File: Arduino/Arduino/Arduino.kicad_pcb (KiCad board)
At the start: 2 copper layers, 98 parts, among them J1 Conn_01x08_Socket, J10 USB_B_Mini, J2 Conn_01x08_Socket, J3 Conn_01x06_Socket, J4 Conn_01x10_Socket, J5 Conn_01x02_Socket, J6 Conn_02x03_Odd_Even, J7 Conn_02x03_Odd_Even, J8 Conn_01x02_Socket, J9 Conn_01x02_Socket, P1 USB_C_Plug_USB2.0, Q1 MMBT3904, Q2 MMBT3904, Q3 MMBT3904, Q4 MMBT3904, Q5 MMBT3904, Q6 MMBT3904, SW1 SW_Push, SW2 SW_Push, SW3 SW_Push, SW4 SW_Push, SW5 SW_Push, SW6 SW_Push, U1 LM1117DT-3.3, U2 TPS61087DSCR, U3 FT232RL, U4 ATxmega32A4U-A, U5 HC-05, U6 L293D

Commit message: Primera versión del Arduino sin completar el Ruteo
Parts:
- removed P1: USB_C_Plug_USB2.0, Connector_USB:USB_C_Receptacle_GCT_USB4125-xx-x_6P_TopMnt_Horizontal
- added H1: MountingHole_Pad, MountingHole:MountingHole_3.2mm_M3_DIN965_Pad, F.Cu at (205.0, 32.5)
- added H2: MountingHole_Pad, MountingHole:MountingHole_3.2mm_M3_DIN965_Pad, F.Cu at (256.3, 47.7)
- added H3: MountingHole_Pad, MountingHole:MountingHole_3.2mm_M3_DIN965_Pad, F.Cu at (256.4, 75.7)
- added H4: MountingHole_Pad, MountingHole:MountingHole_3.2mm_M3_DIN965_Pad, F.Cu at (204.3, 80.8)
- C14, C6, C7, D1, D2, R1, R10, R11, R14, R15, R16, R17, R18, R19, R2, R20, R21, R22, R23, R24, R25, R26, R27, R28, R29, R3, R30, R31, R32, R33, R34, R35, R36, R4, R5, R6, R7, R8, R9, U1, U3: moved to B.Cu
- D5: footprint Diode_SMD:D_SMC -> Diode_SMD:D_SMA; moved to B.Cu
- SW1, SW2, SW3, SW4, SW5, SW6: footprint Button_Switch_THT:SW_Tactile_Straight_KSA0Axx1LFTR -> Button_Switch_SMD:SW_SPST_EVQP2_MiddlePushTravel_H2.5mm
- moved SW6 161.7 mm to (250.0, 68.0)
- moved SW5 161.3 mm to (250.0, 62.7)
- moved SW4 160.9 mm to (250.0, 57.4)
- moved SW3 160.6 mm to (250.0, 52.1)
- moved RV1 157.7 mm to (239.8, 51.3), turned to -90 degrees
- moved SW1 141.2 mm to (230.6, 53.8), turned to 90 degrees
- moved J10 131.4 mm to (196.2, 35.9), turned to -90 degrees
- moved J6 131.3 mm to (246.0, 37.0), turned to 90 degrees
- moved C15 126.9 mm to (256.4, 52.1), turned to -90 degrees
- moved J8 126.8 mm to (251.8, 75.7), turned to 180 degrees
- moved C16 126.5 mm to (256.4, 57.4), turned to -90 degrees
- moved C17 126.2 mm to (256.4, 62.7), turned to -90 degrees
- moved C18 126.0 mm to (256.4, 68.0), turned to -90 degrees
- moved R26 125.8 mm to (256.4, 52.1), turned to -90 degrees
- moved D13 125.7 mm to (208.1, 58.4)
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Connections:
- C3 pad 1: Net-(D5-K) -> +12V
- D5 pad 1: Net-(D5-K) -> +12V
- R4 pad 1: Net-(D5-K) -> +12V
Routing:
- net +5V: track 0.00 -> 120.1 mm, vias 0 -> 3
- net +3.3V: track 0.00 -> 107.1 mm, vias 0 -> 1
- net +12V: track 0.00 -> 53.9 mm, vias 0 -> 1
- net /RESET: track 0.00 -> 48.3 mm
- net /PD0: track 0.00 -> 28.3 mm
- net /3A: track 0.00 -> 19.2 mm, vias 0 -> 2
- net VBUS: track 0.00 -> 17.5 mm, vias 0 -> 2
- net Net-(J9-Pin_1): track 0.00 -> 13.5 mm
- net /2A: track 0.00 -> 12.7 mm, vias 0 -> 1
- net /1A: track 0.00 -> 10.4 mm, vias 0 -> 1
- net Net-(D5-A): track 0.00 -> 10.1 mm, vias 0 -> 1
- net Net-(U3-3V3OUT): track 0.00 -> 9.95 mm
- net Net-(U3-~{RESET}): track 0.00 -> 9.22 mm
- net /PD3: track 0.00 -> 9.03 mm
- net /PD2: track 0.00 -> 9.03 mm
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- added copper zone on B.Cu, net GND
- added copper zone on F.Cu, net GND
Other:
- board outline added: 68.8 x 53.6 mm

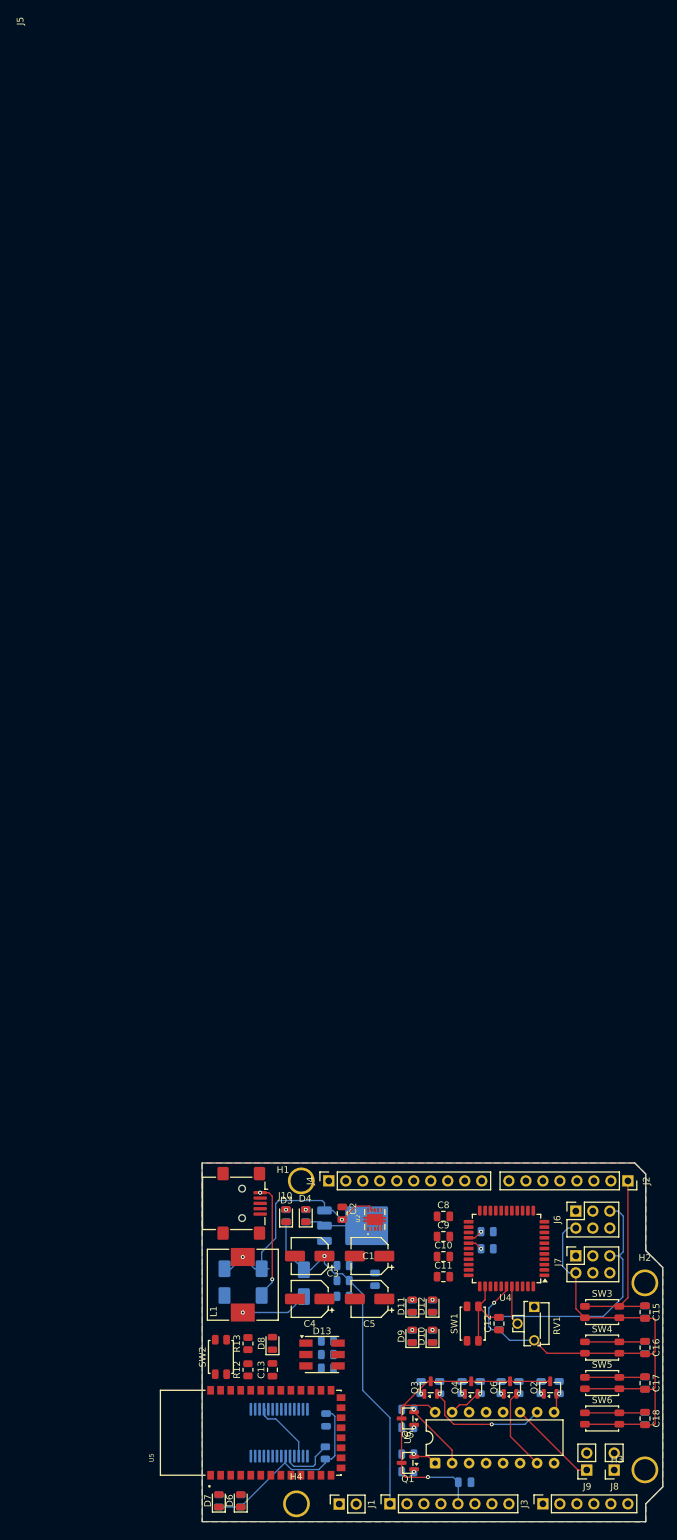
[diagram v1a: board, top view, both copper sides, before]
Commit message: Segunda Versión casi finalizada, falta enrutar detalles y gnd
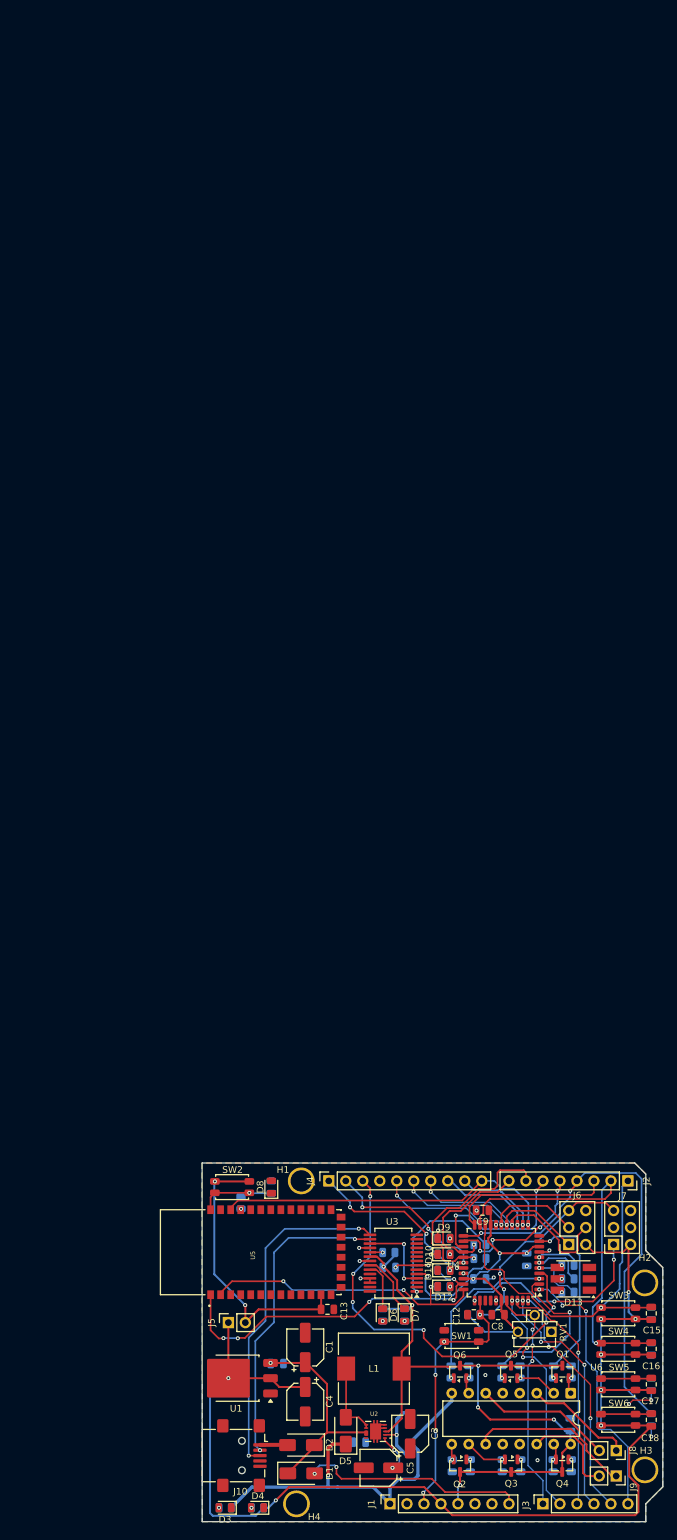
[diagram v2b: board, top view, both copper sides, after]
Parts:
- C10, C11, C2, R12, R13: moved to B.Cu
- D1, D2, D5, U1, U3: moved to F.Cu
- moved D3 44.6 mm to (193.6, 81.3), turned to 180 degrees
- moved R2 44.6 mm to (193.6, 81.3), turned to 180 degrees
- moved D4 44.3 mm to (198.4, 81.3), turned to 180 degrees
- moved R1 44.2 mm to (198.5, 81.3), turned to 180 degrees
- moved R8 39.3 mm to (220.4, 52.5), turned to -90 degrees
- moved D7 39.3 mm to (220.4, 52.5), turned to -90 degrees
- moved D13 39.2 mm to (245.7, 47.1), turned to 180 degrees
- moved R36 39.1 mm to (244.8, 45.1), turned to 180 degrees
- moved J10 37.7 mm to (196.1, 73.5)
- moved R35 37.7 mm to (244.8, 47.1), turned to 180 degrees
- moved R34 36.7 mm to (244.8, 49.1), turned to 180 degrees
- moved R7 35.0 mm to (217.2, 52.5), turned to -90 degrees
- moved D6 34.9 mm to (217.2, 52.5), turned to -90 degrees
- moved J5 31.8 mm to (194.1, 53.7)
- moved U2 31.7 mm to (216.1, 69.9), turned to 180 degrees
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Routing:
- net +3.3V: track 107.1 -> 231.5 mm, vias 1 -> 11
- net /PD3: track 9.03 -> 77.6 mm, vias 0 -> 2
- net /AREF: track 0.00 -> 64.4 mm, vias 0 -> 6
- net /BT_TX: track 0.00 -> 52.9 mm, vias 0 -> 5
- net /BT_STATE: track 0.00 -> 51.1 mm, vias 0 -> 1
- net /D+: track 0.00 -> 51.0 mm, vias 0 -> 2
- net /PD1: track 9.03 -> 58.8 mm, vias 0 -> 1
- net /D-: track 0.00 -> 46.3 mm, vias 0 -> 2
- net /BT_RX: track 0.00 -> 43.9 mm, vias 0 -> 3
- net +3.3VP: track 0.00 -> 42.5 mm, vias 0 -> 2
- net /A5: track 0.00 -> 40.9 mm, vias 0 -> 3
- net /A3: track 0.00 -> 36.6 mm, vias 0 -> 3
- net /A2: track 0.00 -> 36.2 mm, vias 0 -> 2
- net /A4: track 0.00 -> 36.1 mm, vias 0 -> 3
- net /A1: track 0.00 -> 34.9 mm, vias 0 -> 3
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
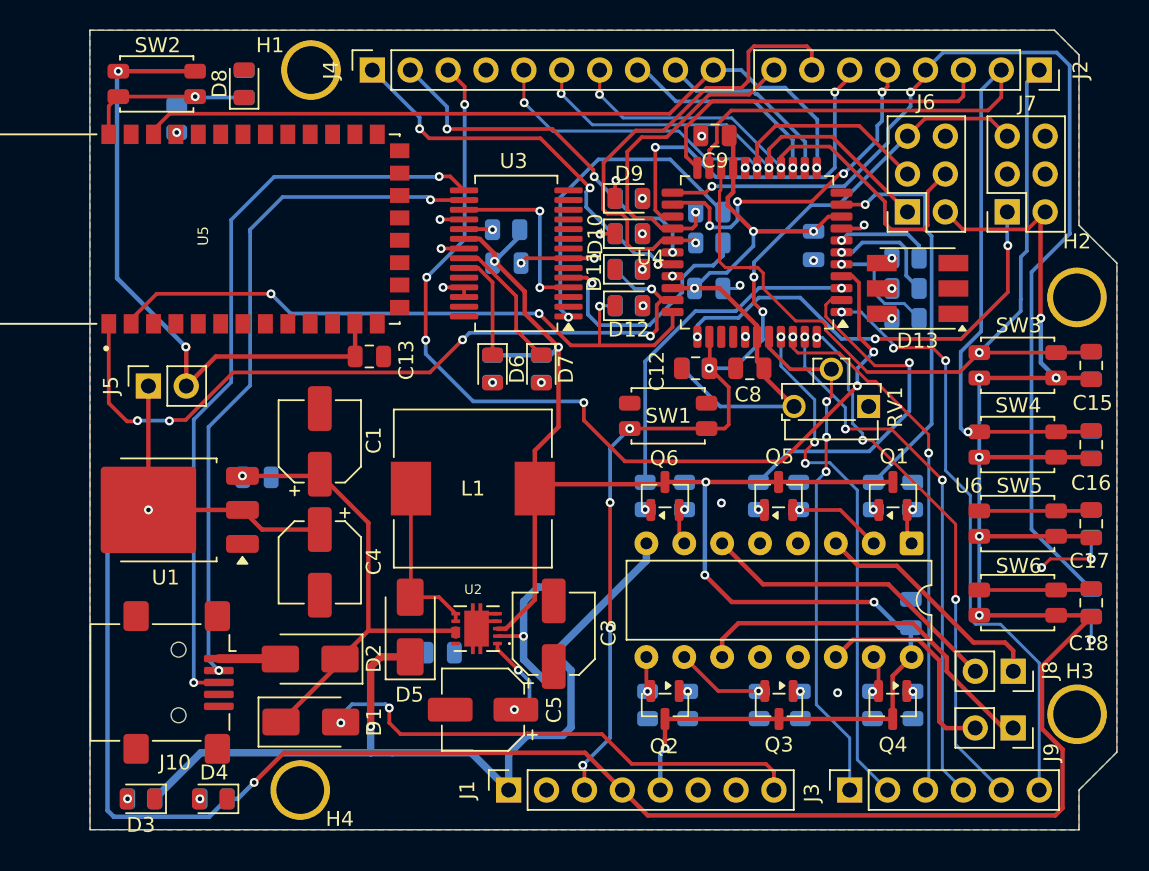
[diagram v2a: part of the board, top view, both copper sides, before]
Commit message: Diseño completo del Arduino sin errores v0.2
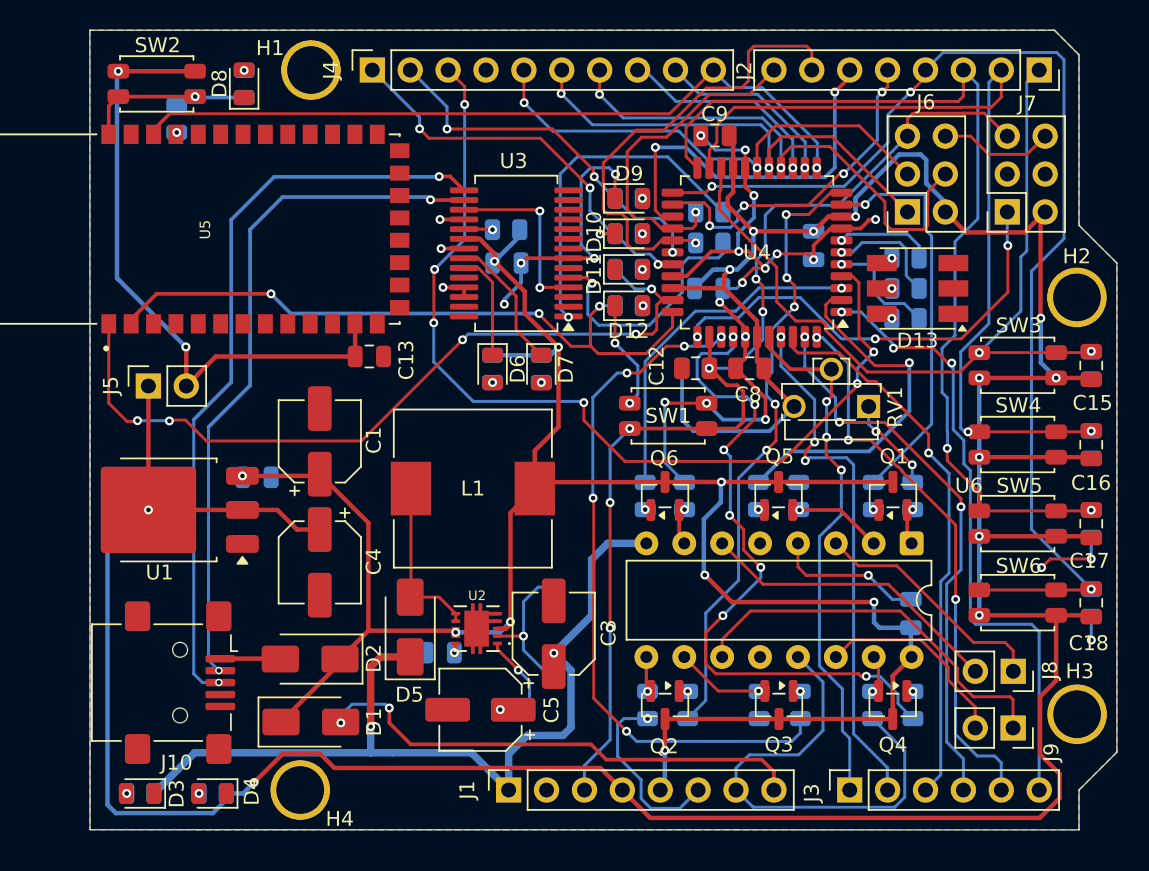
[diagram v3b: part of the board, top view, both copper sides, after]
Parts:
- moved D3 0.36 mm to (193.5, 81.0)
- moved D4 0.36 mm to (198.4, 81.0)
- moved R1 0.36 mm to (198.4, 81.0)
- moved R2 0.36 mm to (193.6, 81.0)
- moved C5 0.17 mm to (216.4, 75.4)
- moved R3 0.14 mm to (218.6, 75.4)
- moved J10 0.10 mm to (196.2, 73.5)
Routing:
- net GND: track 25.9 -> 166.9 mm, vias 19 -> 31
- net /MOT2_A: track 0.00 -> 46.7 mm, vias 0 -> 5
- net /MOT2_B: track 0.00 -> 46.0 mm, vias 0 -> 7
- net /MOT2_PWM: track 0.00 -> 41.8 mm, vias 0 -> 5
- net /PD2: track 31.8 -> 64.2 mm, vias 0 -> 2
- net +3.3V: track 231.5 -> 247.4 mm, vias 11 -> 12
- net +5V: track 143.3 -> 148.5 mm, vias 8 -> 9
- net /RESET: track 70.5 -> 74.5 mm, vias 7 -> 6
- net Net-(J9-Pin_1): track 24.6 -> 27.1 mm
- net +12V: track 57.5 -> 58.9 mm, vias 1 -> 2
- net /A5: track 40.9 -> 42.2 mm
- net /MISO: track 30.6 -> 31.9 mm
- net /A4: track 36.1 -> 37.3 mm
- net /PD0: track 56.3 -> 55.1 mm, vias 1 -> 2
- net /MOSI: track 33.9 -> 35.1 mm
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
